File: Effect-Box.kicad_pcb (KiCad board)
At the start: 6 copper layers, 178.6 x 140 mm, 161 parts, among them J1 Conn_02x07_Odd_Even, J10 Power pins, J2 26642801RP2, J3 FH12A-10S-0.5SH55, J5 Conn_ARM_JTAG_SWD_20, J6 26642801RP2, J7 AudioJack3, J8 AudioJack3, J9 PJ-006A-SMT, SW0 SW_Push, SW1 SW_Push, SW2 SW_Push, SW3 SW_Push, SW4 SW_Push, SW5 SW_Push, SW6 SW_Push, U1 TPS54325, U10 LM7805SX_NOPB, U2 TPS54294, U3 XC7A100T-FTG256, U4 S25FL1, U5 SiT2024B, U7 EFM32GG942F1024, U8 INA1651IPW, U9 PCM3003E

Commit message: Start fixing PCB
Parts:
- moved C10 0.32 mm to (159.1, 60.5)
- moved C8 0.32 mm to (163.9, 60.5)
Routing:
- net PWR_IN: track 168.6 -> 44.7 mm
- net +3V3: track 176.6 -> 170.0 mm, vias 39 -> 35
- net GND: track 410.3 -> 406.7 mm, vias 157 -> 155
- added copper zone on VCC.Cu, net +1V8
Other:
- net class High current: trace_width 1 -> 1.5

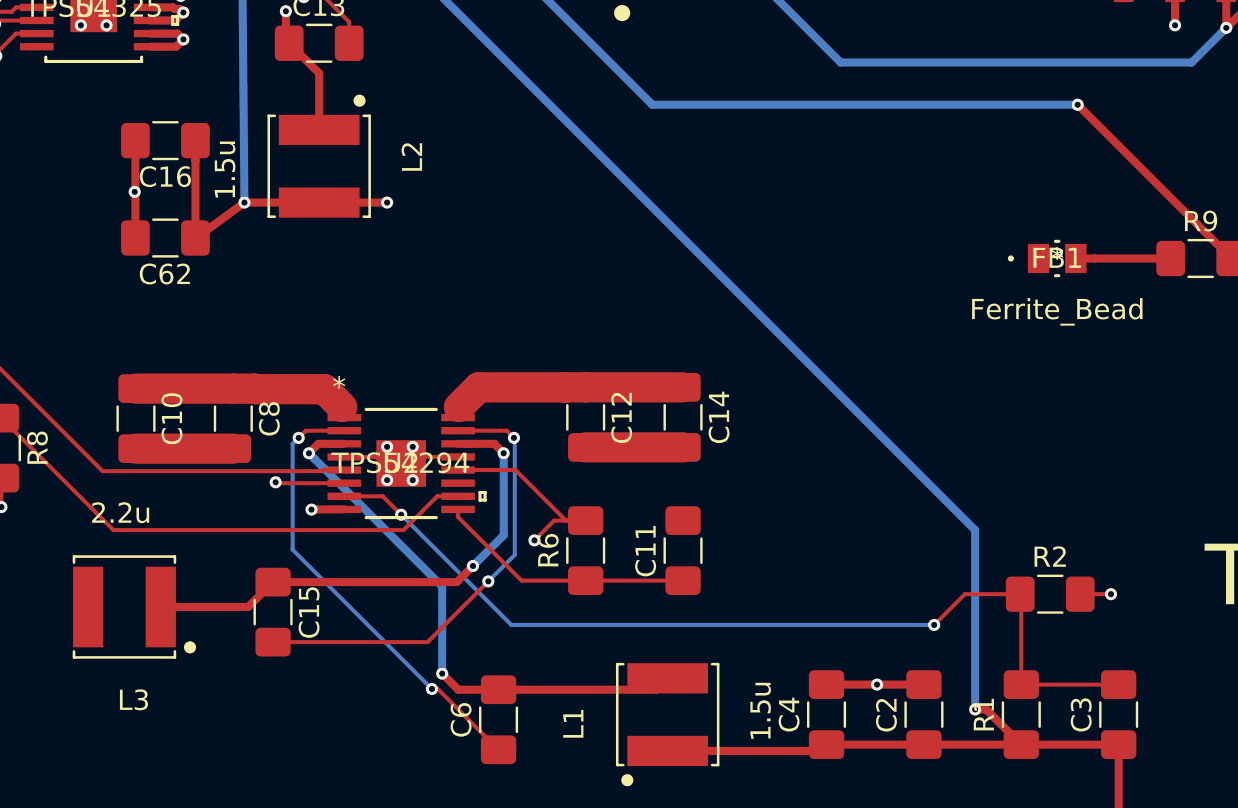
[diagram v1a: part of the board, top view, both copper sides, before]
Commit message: Add new filled zones
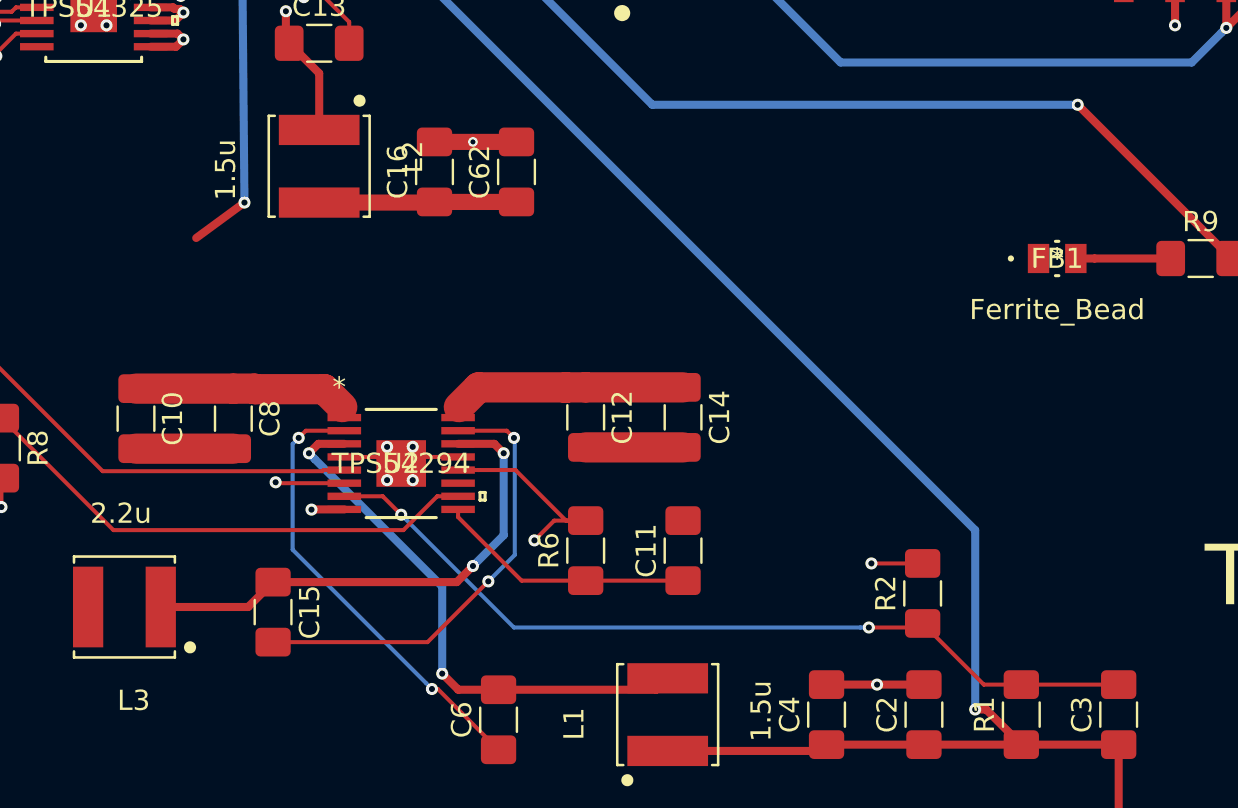
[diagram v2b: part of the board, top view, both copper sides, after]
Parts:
- moved C62 17.7 mm to (177.9, 48.3), turned to 90 degrees
- moved C16 13.4 mm to (173.9, 48.3), turned to 90 degrees
- moved R2 6.32 mm to (198.1, 69.2), turned to 90 degrees
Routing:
- net +1V0: track 245.6 -> 173.5 mm, vias 11 -> 10
- net Net-(C3-Pad2): track 46.1 -> 42.4 mm
- added copper zone on VCC.Cu, net PWR_IN
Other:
- net class Semi-high current: trace_width 0.4 -> 0.8

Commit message: Fix PSU stuff
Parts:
- moved FB1 7.63 mm to (211.8, 55.3), turned to 90 degrees
- moved C78 6.94 mm to (238.0, 60.9)
- moved C18 6.66 mm to (151.2, 71.2), turned to 270 degrees
- moved C1 6.00 mm to (202.2, 40.2), turned to 270 degrees
- moved C17 5.35 mm to (218.4, 40.0), turned to 270 degrees
- moved R9 2.69 mm to (211.8, 49.9), turned to 90 degrees
- moved C19 1.58 mm to (144.6, 71.2), turned to 270 degrees
- moved C77 1.27 mm to (238.0, 57.4)
- moved L1 0.47 mm to (185.0, 75.2), turned to 180 degrees
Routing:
- net +3V3: track 170.0 -> 318.5 mm, vias 35 -> 37
- net GND: track 406.9 -> 469.8 mm, vias 155 -> 170
- net PWR_IN: track 44.7 -> 99.0 mm, vias 0 -> 14
- net +3.3VA: track 85.8 -> 121.0 mm, vias 8 -> 7
- net +5VA: track 84.1 -> 106.0 mm, vias 4 -> 1
- net +1V8: track 168.0 -> 156.9 mm, vias 7 -> 8
- net Net-(C6-Pad2): track 27.3 -> 24.1 mm
- net Net-(C13-Pad1): track 15.2 -> 12.6 mm, vias 2 -> 0
- net /FPGA/FPGA_pinout_16: track 52.7 -> 54.4 mm
- net Net-(FB1-Pad2): track 4.70 -> 3.07 mm
- net Net-(R5-Pad1): track 40.7 -> 42.2 mm, vias 1 -> 2
- net +1V0: track 173.5 -> 172.8 mm, vias 10 -> 12
- net Net-(C13-Pad2): track 11.3 -> 10.8 mm, vias 2 -> 0
- added copper zone on F.Cu, net GND

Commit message: More
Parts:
- moved C46 5.93 mm to (210.0, 112.9)
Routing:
- net GND: track 469.8 -> 354.8 mm, vias 170 -> 161
- net +1V0: track 172.8 -> 79.1 mm, vias 12 -> 7
- net +1V8: track 156.9 -> 105.9 mm, vias 8 -> 6
- net +3V3: track 318.5 -> 280.0 mm, vias 37 -> 27

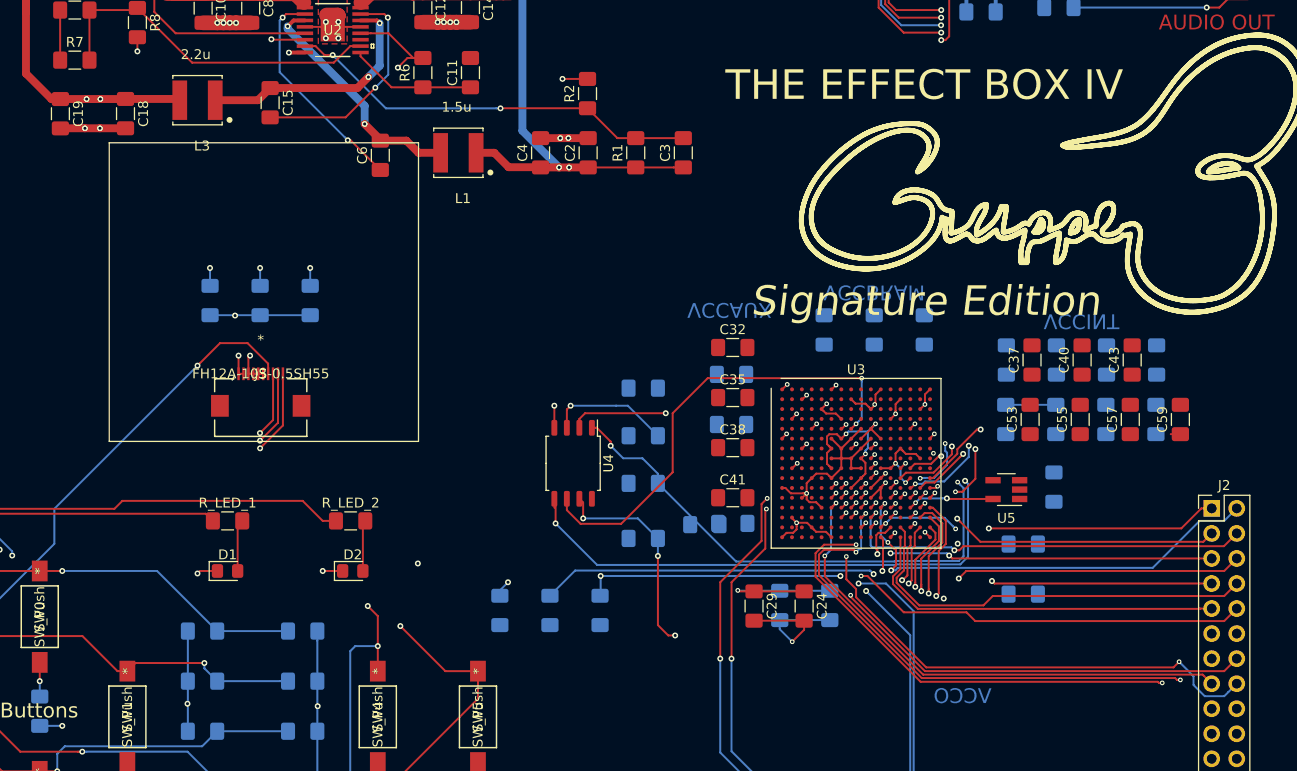
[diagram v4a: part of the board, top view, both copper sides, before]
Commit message: Fix FPGA caps
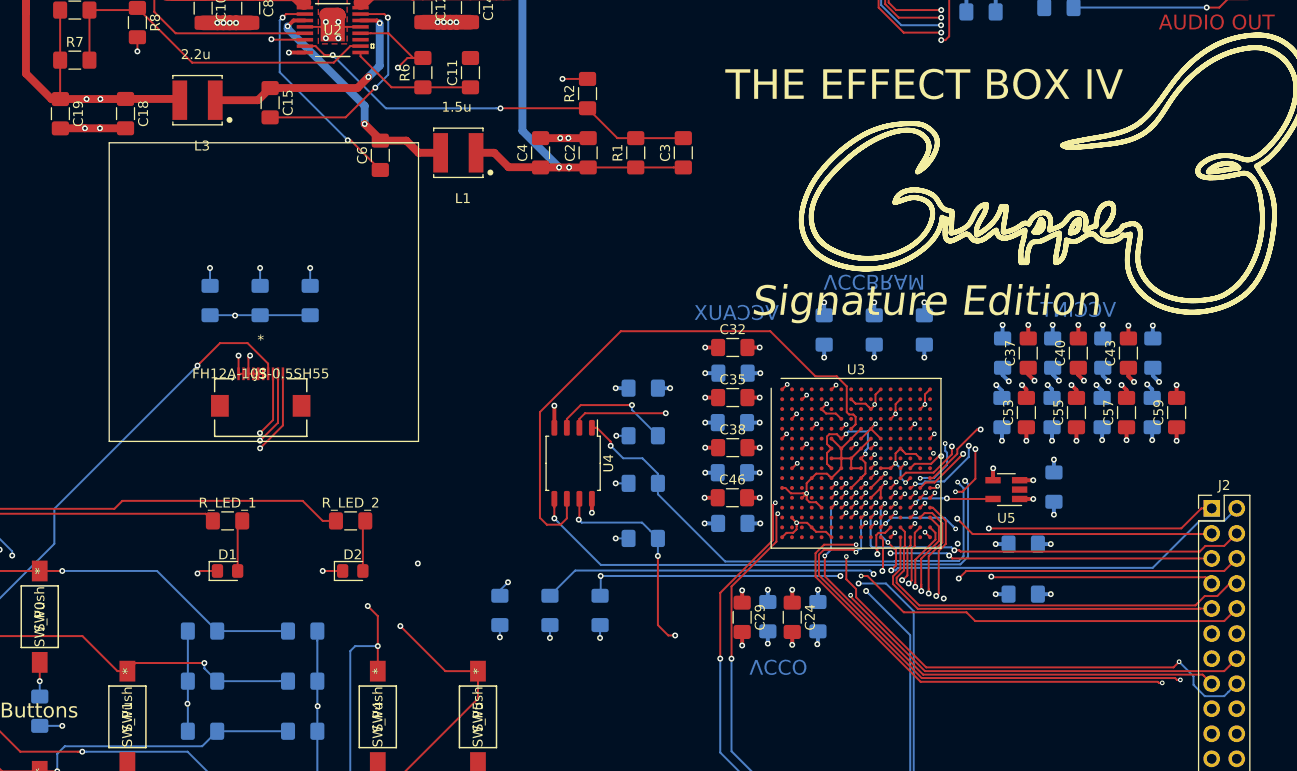
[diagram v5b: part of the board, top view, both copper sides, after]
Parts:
- C41: moved to B.Cu
- C46: moved to F.Cu
- moved C46 3.91 mm to (212.8, 110.2)
- moved C41 2.54 mm to (212.8, 107.6)
- moved C24 1.66 mm to (218.8, 122.3)
- moved C36 1.66 mm to (221.4, 122.2)
- moved C29 1.66 mm to (213.7, 122.3)
- moved C33 1.66 mm to (216.3, 122.2)
- moved C21 0.80 mm to (255.4, 95.5)
- moved C26 0.80 mm to (250.3, 95.5)
- moved C30 0.80 mm to (245.2, 95.5)
- moved C34 0.80 mm to (240.2, 95.5)
- moved C37 0.80 mm to (242.8, 95.5)
- moved C40 0.80 mm to (247.8, 95.5)
- moved C43 0.80 mm to (252.9, 95.5)
- moved C45 0.80 mm to (255.3, 101.5)
- moved C47 0.80 mm to (250.3, 101.5)
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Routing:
- net GND: track 354.8 -> 381.5 mm, vias 161 -> 195
- net +1V0: track 79.1 -> 104.1 mm, vias 7 -> 25
- net +3V3: track 280.0 -> 292.5 mm, vias 27 -> 45
- net Net-(U3-PadE8): track 46.8 -> 57.9 mm, vias 2 -> 0
- net +1V8: track 105.9 -> 113.7 mm, vias 6 -> 12
- net Net-(R16-Pad2): track 58.0 -> 51.6 mm
- net Net-(J1-Pad4): track 61.7 -> 60.8 mm
- net /FPGA/FPGA_pinout_3: track 34.7 -> 34.1 mm
- net Net-(R15-Pad2): track 59.9 -> 60.6 mm

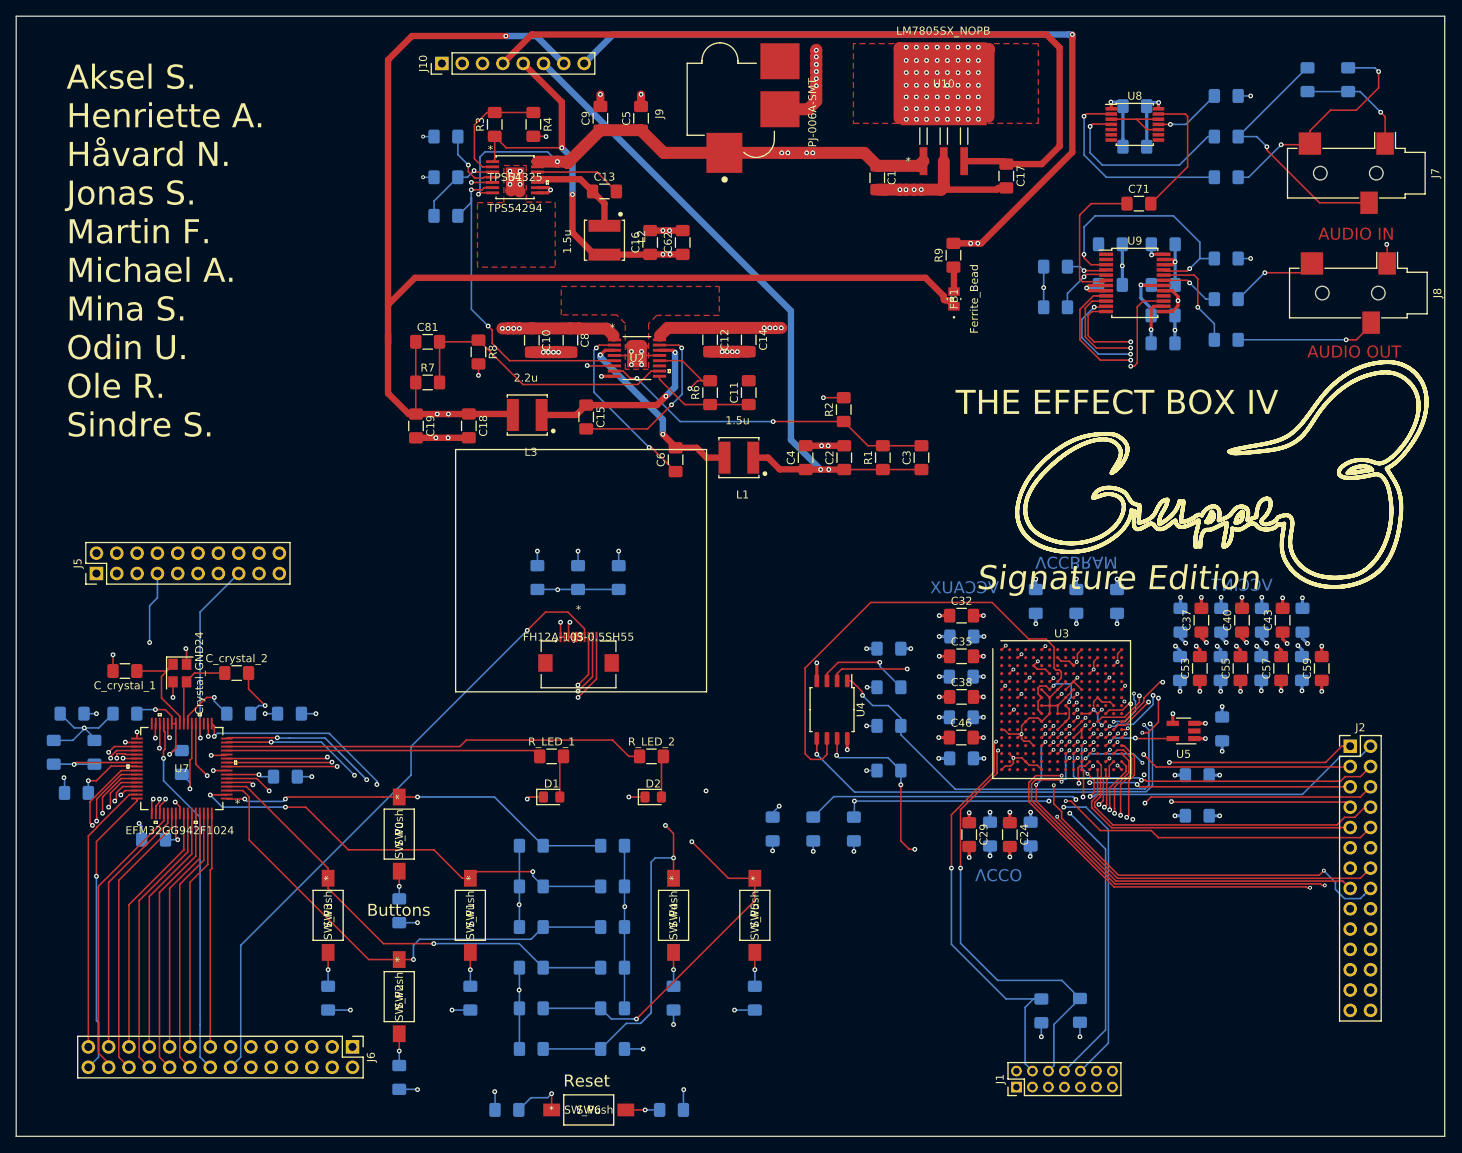
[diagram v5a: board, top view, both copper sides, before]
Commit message: Fix FPGA traces
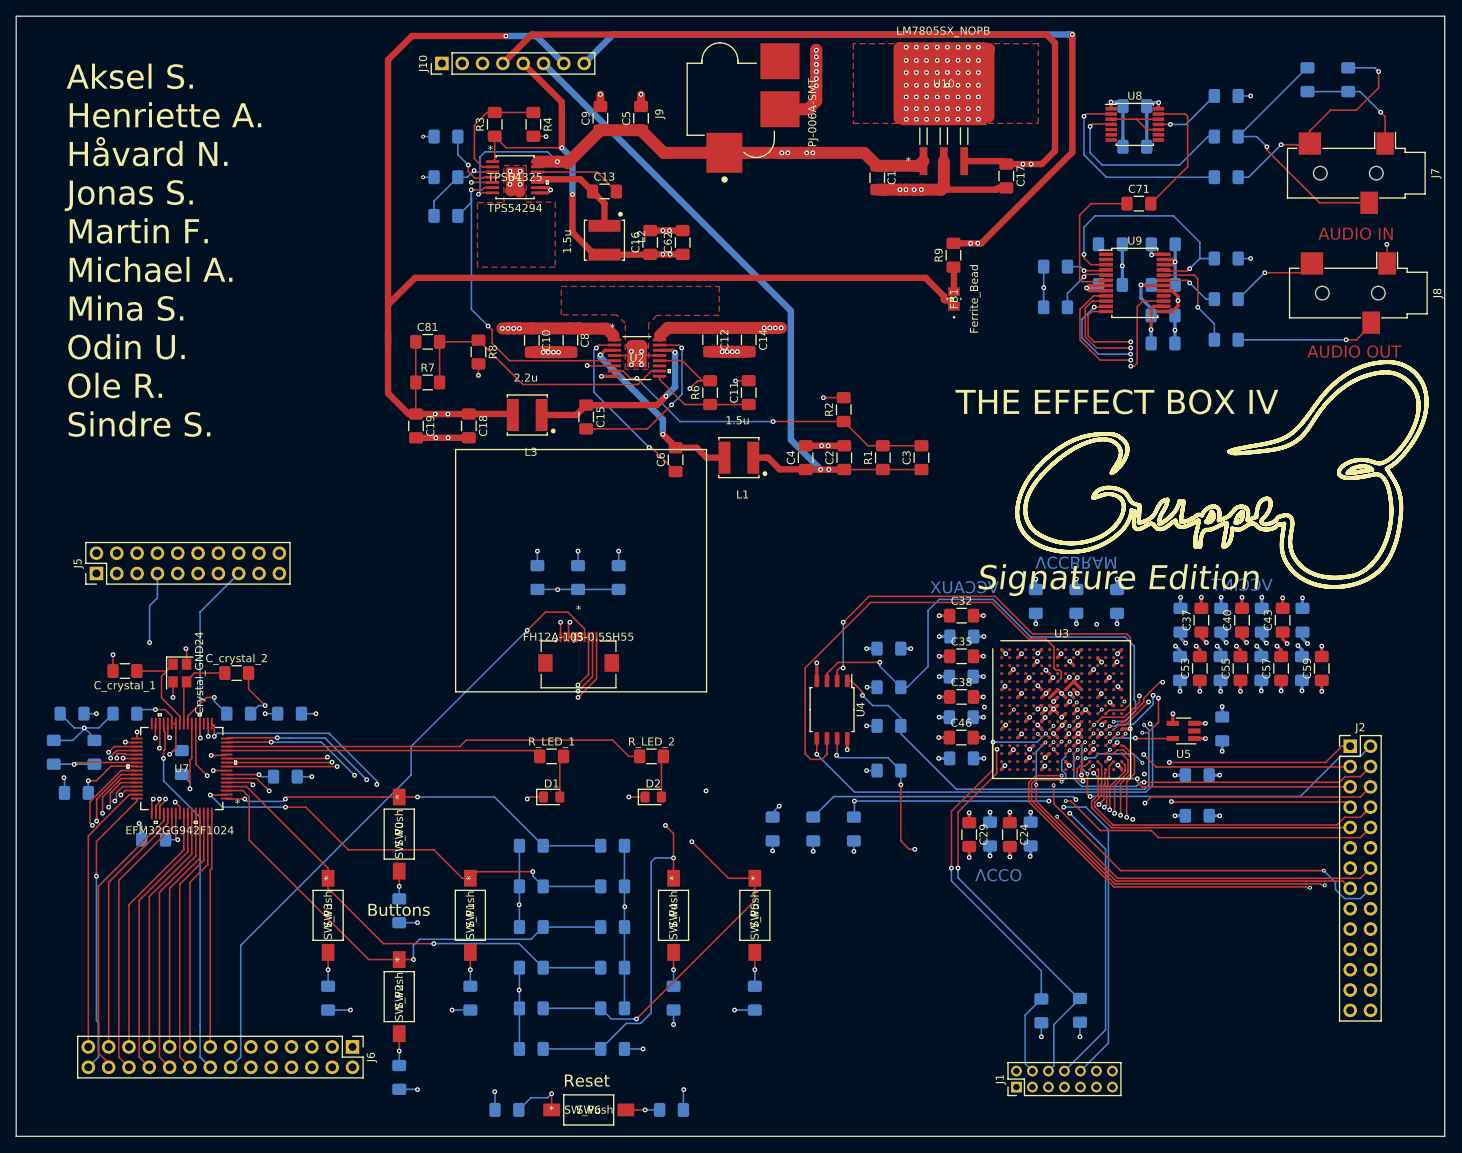
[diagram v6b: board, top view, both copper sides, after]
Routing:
- net GND: track 381.5 -> 355.2 mm, vias 195 -> 217
- net Net-(U3-PadJ14): track 43.5 -> 59.1 mm
- net Net-(R16-Pad2): track 51.6 -> 64.0 mm, vias 3 -> 2
- net Net-(J1-Pad6): track 65.3 -> 59.3 mm
- net Net-(J1-Pad4): track 60.8 -> 56.9 mm
- net +3V3: track 292.5 -> 289.0 mm
- net +1V0: track 104.1 -> 106.5 mm, vias 25 -> 28
- net +1V8: track 113.7 -> 115.3 mm, vias 12 -> 13
- net /FPGA/FPGA_pinout_16: track 54.4 -> 53.1 mm
- net /FPGA/FPGA_pinout_5: track 38.2 -> 37.5 mm
- net /FPGA/FPGA_pinout_4: track 42.4 -> 43.1 mm
- net +5VA: track 106.0 -> 105.6 mm, vias 1 -> 3
